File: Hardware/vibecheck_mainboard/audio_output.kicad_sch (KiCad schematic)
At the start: 33 parts, among them J901 PH-313D, U901 RC4580, U902 TPA6111A2

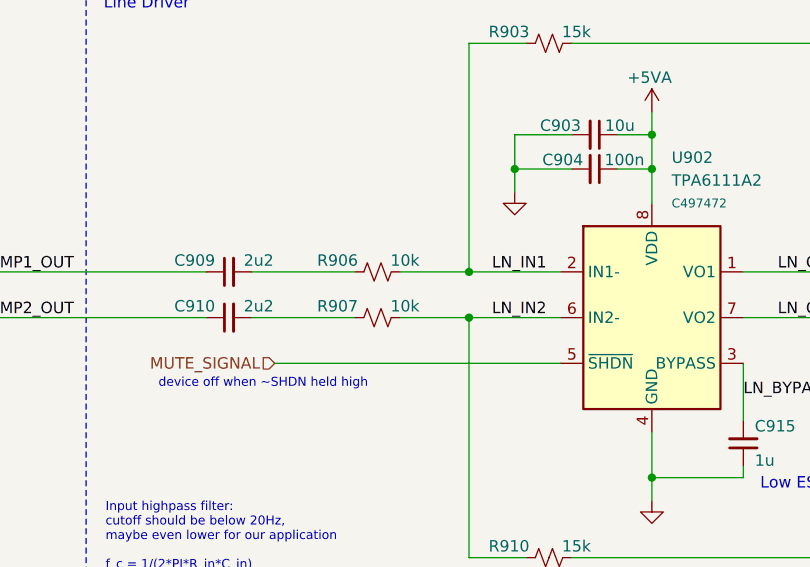
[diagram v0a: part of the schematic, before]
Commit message: VibeCheck mainboard V1.1 sent to JLCPCB
Changes made to main board:
- audio filter/amplifier gain changed from 1.5 to 1. Changed values of R_in and R_f resistors.
- changed sensor labels on board from 'accel 1' ... to 'sensor 0' ... to match firmware
- updated BOM and DNP parts to make sure they matched better reducing warnings in JLCPCB parts selection process
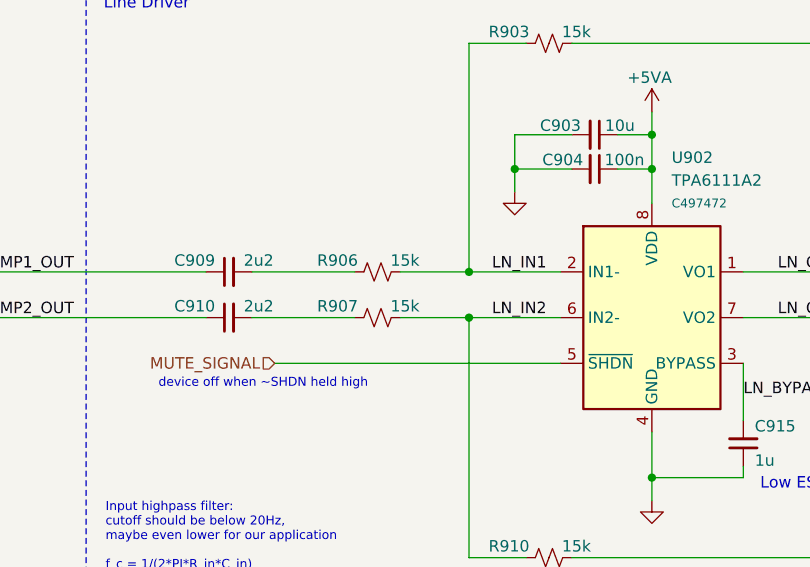
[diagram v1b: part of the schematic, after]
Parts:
- C905, C916: footprint Capacitor_SMD:C_0402_1005Metric_Pad0.74x0.62mm_HandSolder -> Capacitor_SMD:C_0402_1005Metric
- C912: footprint Capacitor_SMD:C_0603_1608Metric -> Capacitor_SMD:C_0402_1005Metric; LCSC (none) -> C307331
- R903, R910: footprint Resistor_SMD:R_0805_2012Metric -> Resistor_SMD:R_0603_1608Metric; LCSC C17475 -> C22809
- R906, R907: value 10k -> 15k; footprint Resistor_SMD:R_0402_1005Metric -> Resistor_SMD:R_0603_1608Metric; LCSC C25744 -> C22809
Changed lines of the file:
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@@
 			)
 		)
-		(property "Footprint" "Capacitor_SMD:C_0603_1608Metric"
+		(property "Footprint" "Capacitor_SMD:C_0402_1005Metric"
 			(at 76.2 125.73 0)
 			(effects
@@
 			)
 		)
-		(property "Datasheet" "~"
+		(property "Datasheet" "https://wmsc.lcsc.com/wmsc/upload/file/pdf/v2/lcsc/2304140030_Samsung-Electro-Mechanics-CL05B104KB54PNC_C307331.pdf"
 			(at 76.2 125.73 0)
 			(effects
@@
 		)
 		(property "Description" "Unpolarized capacitor, small symbol"
+			(at 76.2 125.73 0)
+			(effects
+				(font
+					(size 1.27 1.27)
+				)
+				(hide yes)
+			)
+		)
+		(property "LCSC" "C307331"
 			(at 76.2 125.73 0)
 			(effects
@@
 			)
 		)
-		(property "Footprint" "Resistor_SMD:R_0805_2012Metric"
+		(property "Footprint" "Resistor_SMD:R_0603_1608Metric"
 			(at 181.61 81.28 0)
 			(effects
@@
 			)
 		)
-		(property "Datasheet" "https://wmsc.lcsc.com/wmsc/upload/file/pdf/v2/lcsc/2206010216_UNI-ROYAL-Uniroyal-Elec-0805W8F1502T5E_C17475.pdf"
+		(property "Datasheet" "https://www.lcsc.com/datasheet/lcsc_datasheet_2206010130_UNI-ROYAL-Uniroyal-Elec-0603WAF1502T5E_C22809.pdf"
 			(at 181.61 81.28 0)
 			(effects
@@
 			)
 		)
-		(property "LCSC" "C17475"
+		(property "LCSC" "C22809"
 			(at 181.61 81.28 0)
 			(effects
@@
 			)
 		)
-		(property "Footprint" "Resistor_SMD:R_0805_2012Metric"
+		(property "Footprint" "Resistor_SMD:R_0603_1608Metric"
 			(at 181.61 138.43 0)
 			(effects
@@
 			)
 		)
-		(property "Datasheet" "https://wmsc.lcsc.com/wmsc/upload/file/pdf/v2/lcsc/2206010216_UNI-ROYAL-Uniroyal-Elec-0805W8F1502T5E_C17475.pdf"
+		(property "Datasheet" "https://www.lcsc.com/datasheet/lcsc_datasheet_2206010130_UNI-ROYAL-Uniroyal-Elec-0603WAF1502T5E_C22809.pdf"
 			(at 181.61 138.43 0)
 			(effects
@@
 			)
 		)
-		(property "LCSC" "C17475"
+		(property "LCSC" "C22809"
 			(at 181.61 138.43 0)
 			(effects
@@
 			)
 		)
-		(property "Footprint" "Capacitor_SMD:C_0402_1005Metric_Pad0.74x0.62mm_HandSolder"
+		(property "Footprint" "Capacitor_SMD:C_0402_1005Metric"
 			(at 66.04 147.32 0)
 			(effects
@@
 			)
 		)
-		(property "Value" "10k"
+		(property "Value" "15k"
 			(at 165.608 110.49 90)
 			(effects
@@
 			)
 		)
-		(property "Footprint" "Resistor_SMD:R_0402_1005Metric"
+		(property "Footprint" "Resistor_SMD:R_0603_1608Metric"
 			(at 162.56 111.76 0)
 			(effects
@@
 			)
 		)
-		(property "Datasheet" "https://wmsc.lcsc.com/wmsc/upload/file/pdf/v2/lcsc/2206010100_UNI-ROYAL-Uniroyal-Elec-0402WGF1002TCE_C25744.pdf"
+		(property "Datasheet" "https://www.lcsc.com/datasheet/lcsc_datasheet_2206010130_UNI-ROYAL-Uniroyal-Elec-0603WAF1502T5E_C22809.pdf"
 			(at 162.56 111.76 0)
 			(effects
@@
 			)
 		)
-		(property "LCSC" "C25744"
+		(property "LCSC" "C22809"
 			(at 162.56 111.76 0)
 			(effects
@@
 			)
 		)
-		(property "Value" "10k"
+		(property "Value" "15k"
 			(at 165.608 105.41 90)
 			(effects
@@
 			)
 		)
-		(property "Footprint" "Resistor_SMD:R_0402_1005Metric"
+		(property "Footprint" "Resistor_SMD:R_0603_1608Metric"
 			(at 162.56 106.68 0)
 			(effects
@@
 			)
 		)
-		(property "Datasheet" "https://wmsc.lcsc.com/wmsc/upload/file/pdf/v2/lcsc/2206010100_UNI-ROYAL-Uniroyal-Elec-0402WGF1002TCE_C25744.pdf"
+		(property "Datasheet" "https://www.lcsc.com/datasheet/lcsc_datasheet_2206010130_UNI-ROYAL-Uniroyal-Elec-0603WAF1502T5E_C22809.pdf"
 			(at 162.56 106.68 0)
 			(effects
@@
 			)
 		)
-		(property "LCSC" "C25744"
+		(property "LCSC" "C22809"
 			(at 162.56 106.68 0)
 			(effects
@@
 			)
 		)
-		(property "Footprint" "Capacitor_SMD:C_0402_1005Metric_Pad0.74x0.62mm_HandSolder"
+		(property "Footprint" "Capacitor_SMD:C_0402_1005Metric"
 			(at 66.04 92.71 0)
 			(effects
